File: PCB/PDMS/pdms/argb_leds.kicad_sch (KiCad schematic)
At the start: 19 parts

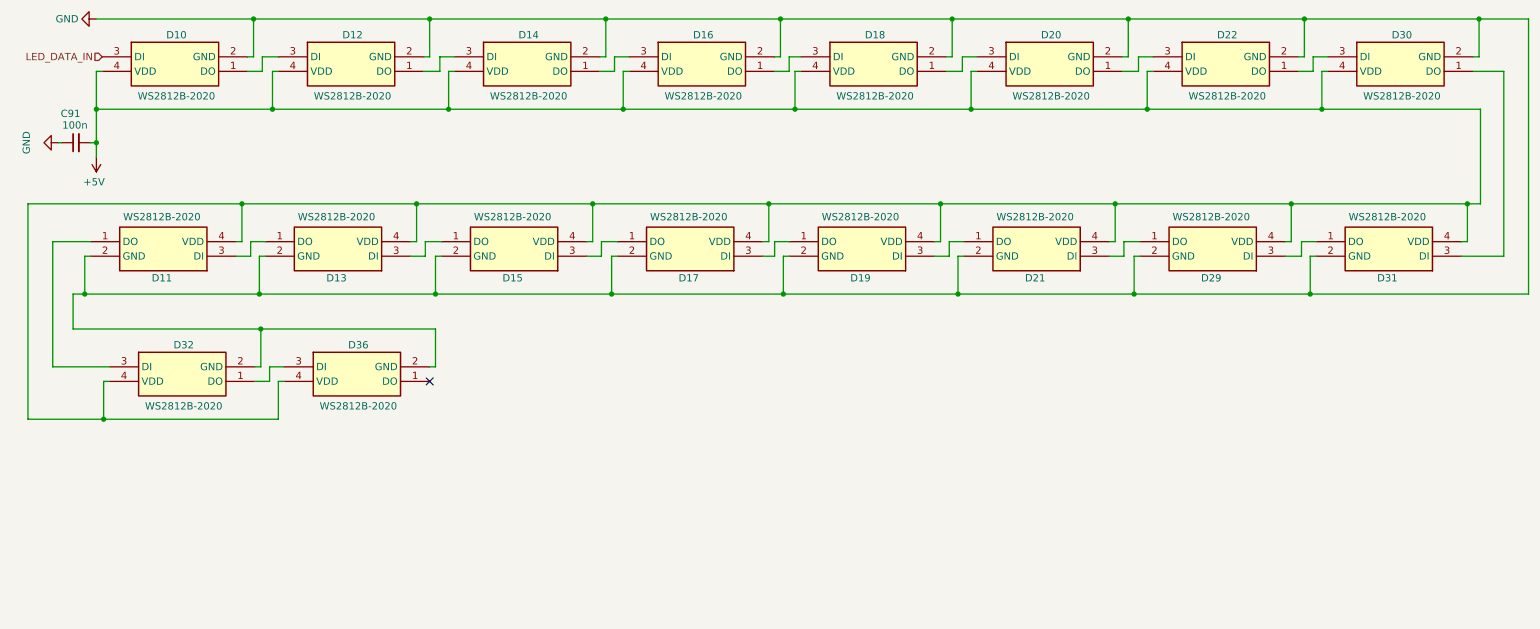
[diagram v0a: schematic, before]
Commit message: PDMS PCB V4.3 modification finished layout - drc clean-up, added external one-wire temp probe
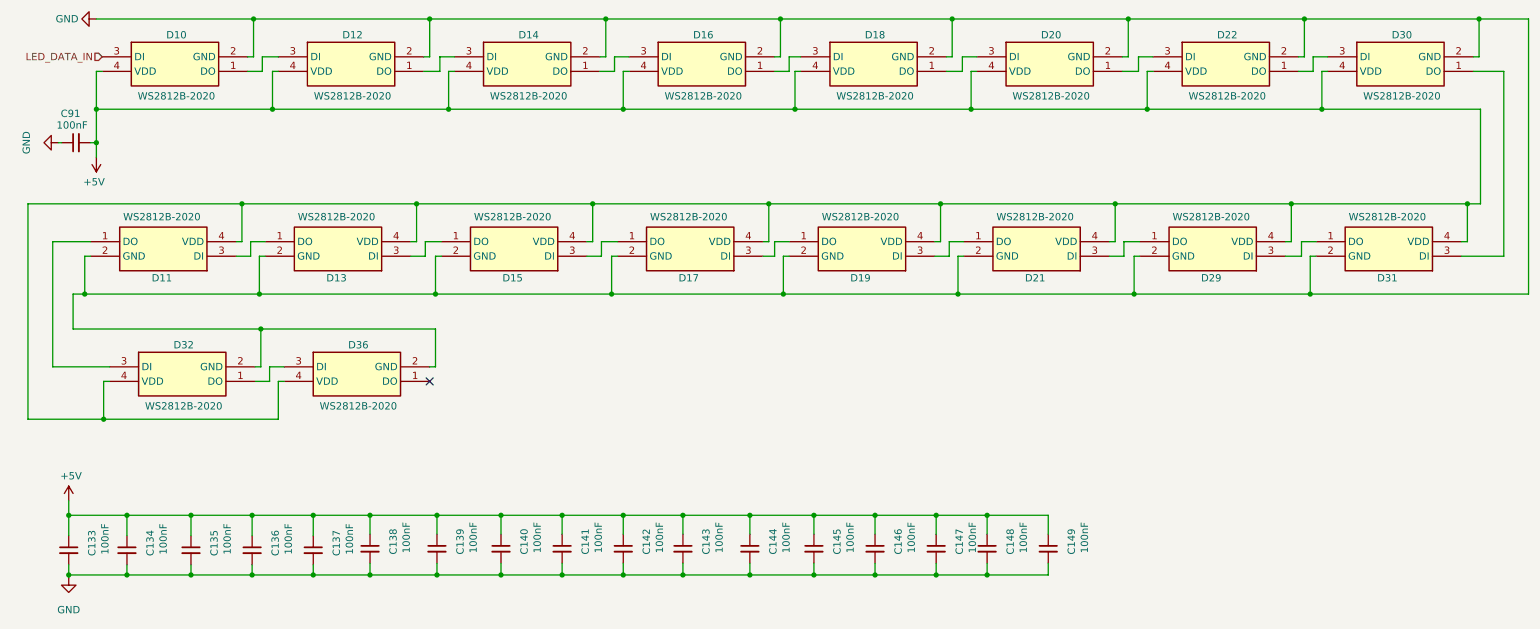
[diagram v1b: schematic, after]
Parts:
- added C133, C134, C135, C136, C137, C138, C139, C140, C141, C142, C143, C144, C145, C146, C147, C148, C149: 100nF, Resistor_SMD:R_0402_1005Metric, symbol Device:C_Small
- C91: value 100n -> 100nF
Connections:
- net +5V: now also C133.1, C134.1, C135.1, C136.1, C137.1, C138.1, C139.1, C140.1, C141.1, C142.1, C143.1, C144.1, C145.1, C146.1, C147.1, C148.1, C149.1
- net GND: now also C133.2, C134.2, C135.2, C136.2, C137.2, C138.2, C139.2, C140.2, C141.2, C142.2, C143.2, C144.2, C145.2, C146.2, C147.2, C148.2, C149.2
